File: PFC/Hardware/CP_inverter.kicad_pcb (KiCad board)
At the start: 4 copper layers, 380 x 200 mm, 164 parts, among them J1 Weidmueller 1988610000, J2 PGood, J3 PGood, J4 PGood, J5 Power in, J6 Weidmueller 2453690000, Q1 IRLML0030TRPBF, Q2 C3M0060065D, Q3 C3M0060065D, U1 LTV-217-C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

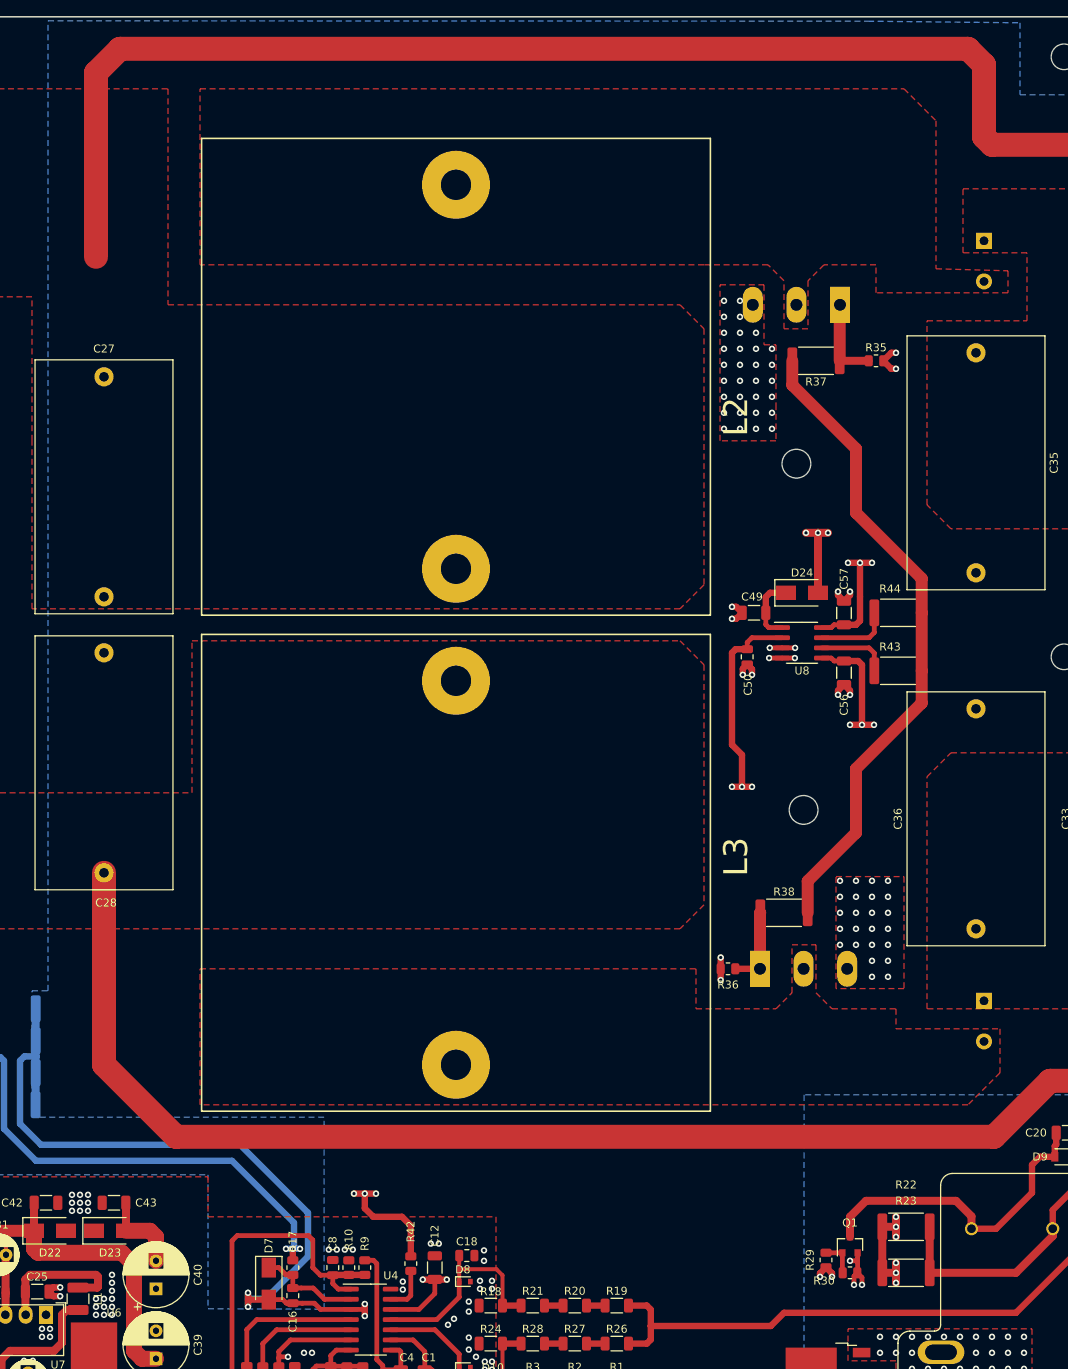
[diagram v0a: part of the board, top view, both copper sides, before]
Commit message: new: PSFB files added
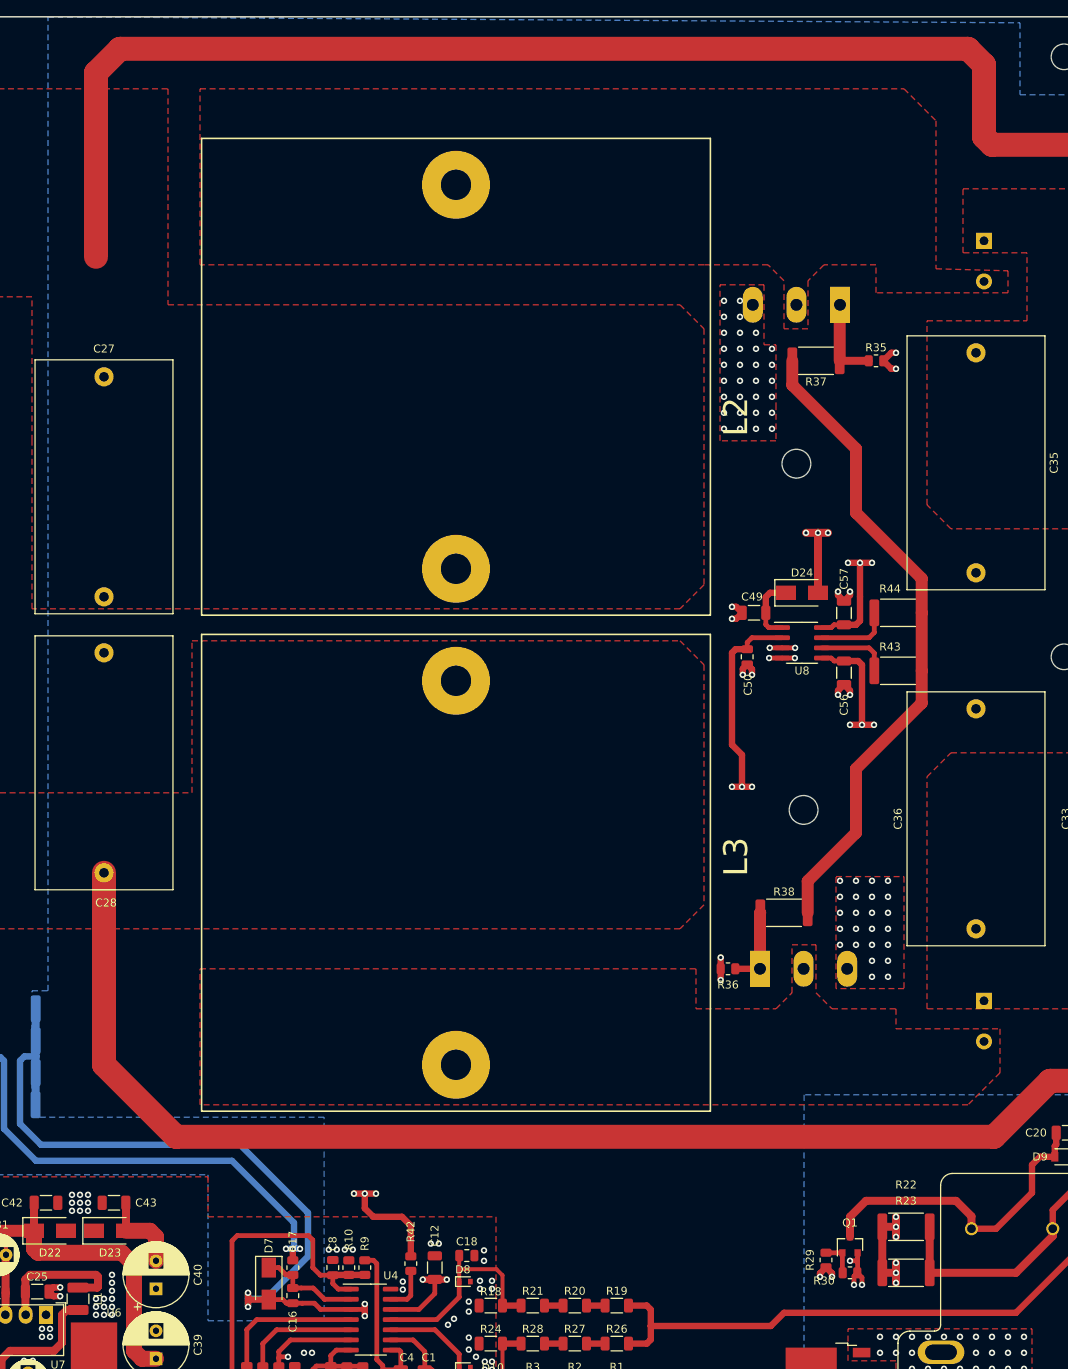
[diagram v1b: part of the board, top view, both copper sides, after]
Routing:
- net VCC: track 378.2 -> 379.2 mm
- added copper zone on In1.Cu, net VCC
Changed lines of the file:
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@@
     (1 In1.Cu signal)
     (2 In2.Cu signal)
-    (31 B.Cu signal hide)
+    (31 B.Cu signal)
     (32 B.Adhes user)
     (33 F.Adhes user)
@@
   )
   (setup
-    (last_trace_width 0.25)
+    (last_trace_width 2)
     (user_trace_width 0.3)
     (user_trace_width 0.5)
@@
   (via (at 172.75 115.5) (size 0.8) (drill 0.4) (layers F.Cu B.Cu) (net 14))
   (segment (start 174.25 115.5) (end 174.25 123) (width 1) (layer F.Cu) (net 14))
-  (segment (start 186 118.5) (end 183 115.5) (width 2) (layer In1.Cu) (net 14))
-  (segment (start 186 141) (end 186 118.5) (width 2) (layer In1.Cu) (net 14))
-  (segment (start 183 115.5) (end 172.75 115.5) (width 2) (layer In1.Cu) (net 14))
-  (segment (start 183 144) (end 186 141) (width 2) (layer In1.Cu) (net 14))
-  (segment (start 147 160) (end 163 144) (width 2) (layer In1.Cu) (net 14))
-  (segment (start 106 160) (end 147 160) (width 2) (layer In1.Cu) (net 14))
-  (segment (start 101 165) (end 106 160) (width 2) (layer In1.Cu) (net 14))
-  (segment (start 163 144) (end 183 144) (width 2) (layer In1.Cu) (net 14))
-  (segment (start 91.5 227.5) (end 101 218) (width 2) (layer In1.Cu) (net 14))
-  (segment (start 91.5 239) (end 91.5 227.5) (width 2) (layer In1.Cu) (net 14))
   (segment (start 184 209.25) (end 184 204.75) (width 2) (layer In1.Cu) (net 14))
   (segment (start 184 204.75) (end 184 201) (width 2) (layer In1.Cu) (net 14))
@@
   (segment (start 126.35 208.85) (end 126.35 211.4) (width 2) (layer In1.Cu) (net 14))
   (segment (start 120 211.25) (end 120 203.5) (width 2) (layer In1.Cu) (net 14))
-  (segment (start 101 202.75) (end 101 165) (width 2) (layer In1.Cu) (net 14))
-  (segment (start 101 218) (end 101 202.75) (width 2) (layer In1.Cu) (net 14))
   (segment (start 179.25 204.75) (end 184 204.75) (width 2) (layer In1.Cu) (net 14))
   (segment (start 172.5 198) (end 179.25 204.75) (width 2) (layer In1.Cu) (net 14))
@@
   (segment (start 120 203.5) (end 120 201) (width 2) (layer In1.Cu) (net 14))
   (segment (start 120 202.5) (end 101.25 202.5) (width 2) (layer In1.Cu) (net 14))
+  (segment (start 91.5 227.5) (end 91.5 227.868002) (width 2) (layer In1.Cu) (net 14))
+  (segment (start 91.5 227.868002) (end 91.5 240) (width 2) (layer In1.Cu) (net 14))
+  (segment (start 106 160) (end 101 165) (width 2) (layer In1.Cu) (net 14))
+  (segment (start 147 160) (end 106 160) (width 2) (layer In1.Cu) (net 14))
+  (segment (start 163 144) (end 147 160) (width 2) (layer In1.Cu) (net 14))
+  (segment (start 101 218) (end 91.5 227.5) (width 2) (layer In1.Cu) (net 14))
+  (segment (start 183 144) (end 163 144) (width 2) (layer In1.Cu) (net 14))
+  (segment (start 101 165) (end 101 218) (width 2) (layer In1.Cu) (net 14))
+  (segment (start 186 141) (end 183 144) (width 2) (layer In1.Cu) (net 14))
+  (segment (start 186 118.5) (end 186 141) (width 2) (layer In1.Cu) (net 14))
+  (segment (start 183 115.5) (end 186 118.5) (width 2) (layer In1.Cu) (net 14))
+  (segment (start 172.75 115.5) (end 183 115.5) (width 2) (layer In1.Cu) (net 14))
   (segment (start 111.55 232.05) (end 112.35 232.05) (width 0.6) (layer F.Cu) (net 15))
   (segment (start 111.05 231.55) (end 111.55 232.05) (width 0.6) (layer F.Cu) (net 15))
@@
     (polygon
       (pts
-        (xy 180.511122 51.550742) (xy 199.5 51.75) (xy 199.5 60.75) (xy 210.5 60.75) (xy 210.5 51.75)
+        (xy 78 51) (xy 199.5 51.75) (xy 199.5 60.75) (xy 210.5 60.75) (xy 210.5 51.75)
         (xy 388.5 51.75) (xy 388.5 177.25) (xy 225 177.25) (xy 225 185.75) (xy 172.511122 185.75)
         (xy 172.5 249.75) (xy 30.5 249.75) (xy 30.5 241.25) (xy 23 241.25) (xy 22.5 195.75)
-        (xy 98 195.75) (xy 97.999092 212.497524) (xy 100.499058 212.506692) (xy 112.511122 212.550742) (xy 112.511122 188.550742)
-        (xy 76 188.550742) (xy 76 172.75) (xy 78 172.75) (xy 78 51.5)
+        (xy 98 195.75) (xy 98 214) (xy 112.511122 214) (xy 112.511122 188.550742) (xy 76 188.550742)
+        (xy 76 172.75) (xy 78 172.75)
       )
     )
@@
       )
     )
+  )
+  (zone (net 14) (net_name VCC) (layer In1.Cu) (hatch edge 0.508)
+    (priority 3)
+    (connect_pads yes (clearance 0.6))
+    (min_thickness 0.254)
+    (fill yes (arc_segments 32) (thermal_gap 0.508) (thermal_bridge_width 0.508))
+    (polygon
+      (pts
+        (xy 93.75 241.75) (xy 89.5 241.75) (xy 89.5 235.75) (xy 93.75 235.75)
+      )
+    )
+  )
+  (zone (net 0) (net_name "") (layer In1.Cu) (hatch edge 0.508)
+    (connect_pads yes (clearance 0.6))
+    (min_thickness 0.254)
+    (keepout (tracks allowed) (vias allowed) (copperpour not_allowed))
+    (fill (arc_segments 32) (thermal_gap 0.508) (thermal_bridge_width 0.508))
+    (polygon
+      (pts
+        (xy 104 213.25) (xy 102.5 213.25) (xy 102.5 209.5) (xy 104 209.5)
+      )
+    )
